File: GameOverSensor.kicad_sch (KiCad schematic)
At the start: 20 parts

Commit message: Changes Serial Port connector to match esp-prog
Both esp-prog and the tag connect cable use even/odd numbering for the
two row connector.
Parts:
- removed J?: Serial Port, symbol Connector_Generic:Conn_02x03_Counter_Clockwise
- added J?: Serial Port, symbol Connector_Generic:Conn_02x03_Odd_Even
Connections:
- net +3V3: now also J?.2 (Pin_2)
- net ESP_BOOT: now also J?.6 (Pin_6)
- net ESP_EN: now also J?.1 (Pin_1)
- net ESP_RX: now also J?.5 (Pin_5)
- net ESP_TX: now also J?.3 (Pin_3)
- net GND: now also J?.4 (Pin_4)

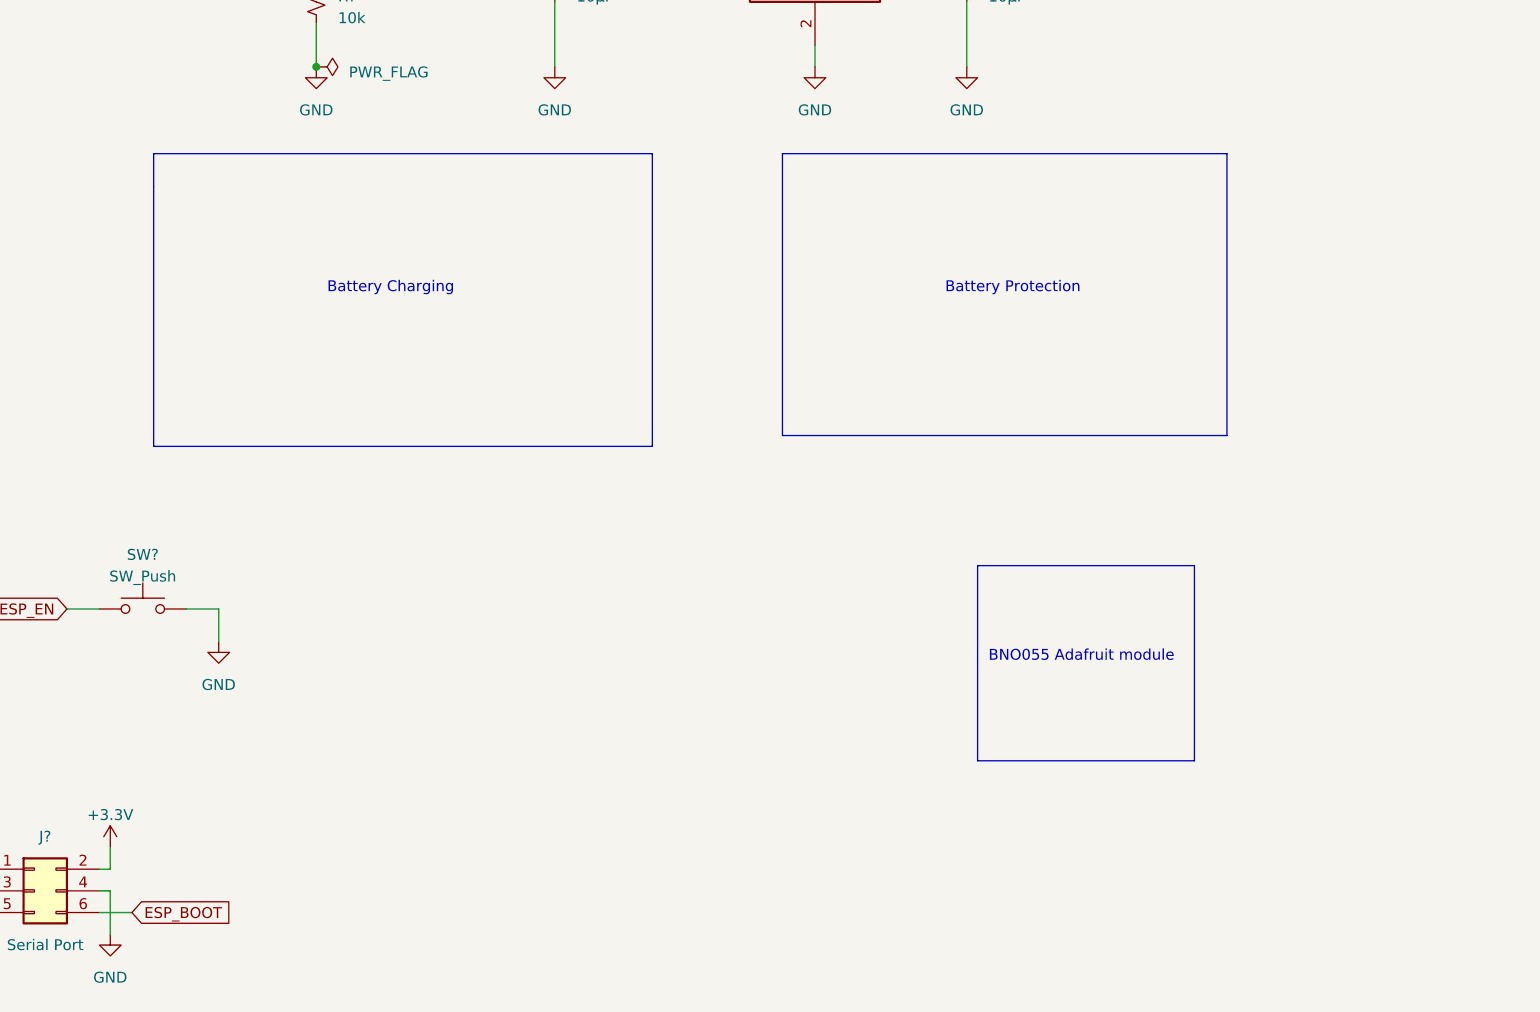
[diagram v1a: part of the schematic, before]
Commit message: Adds battery charging circuit with an MCP73831
The battery will be 400mA, which means we should use 200mA to charge the
battery. This would mean a 5kΩ prog resistor. A 5.1kΩ resistor was
chosen instead to simplify the BOM since we'll already use some of those
in the USB configuration. This means a charging current of approximately
196mA.
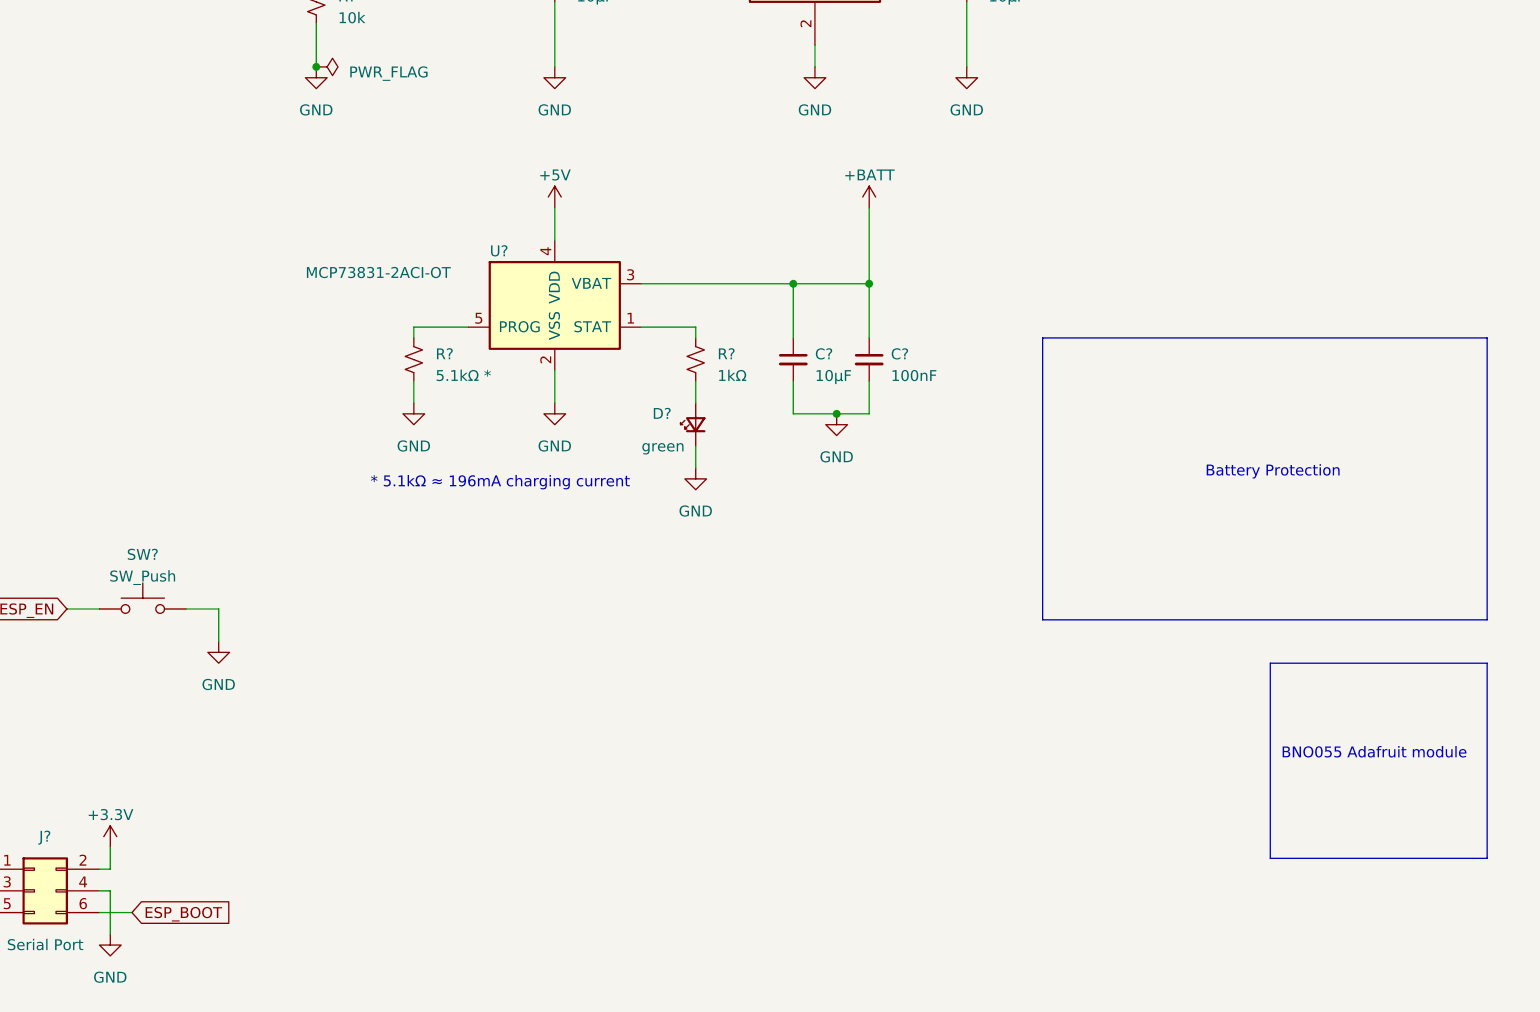
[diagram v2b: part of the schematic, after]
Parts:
- added C?: 10µF, symbol Device:C_Small
- added C?: 100nF, symbol Device:C_Small
- added D?: green, symbol Device:LED_Small
- added R?: 5.1kΩ *, symbol Device:R_Small_US
- added R?: 1kΩ, symbol Device:R_Small_US
- added U?: MCP73831-2ACI-OT, Package_TO_SOT_SMD:SOT-23-5, symbol Battery_Management:MCP73831-2-OT
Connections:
- net +5V: now also U?.4 (VDD)
- net +BATT: now also C?.1, C?.1, U?.3 (VBAT)
- net GND: now also C?.2, C?.2, D?.1 (K), R?.2, U?.2 (VSS)
- new net: R?.1, U?.5 (PROG)
- new net: R?.1, U?.1 (STAT)
- new net: D?.2 (A), R?.2
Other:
- note added: "* 5.1kΩ ≈ 196mA charging current"
- note removed: "Battery Charging"

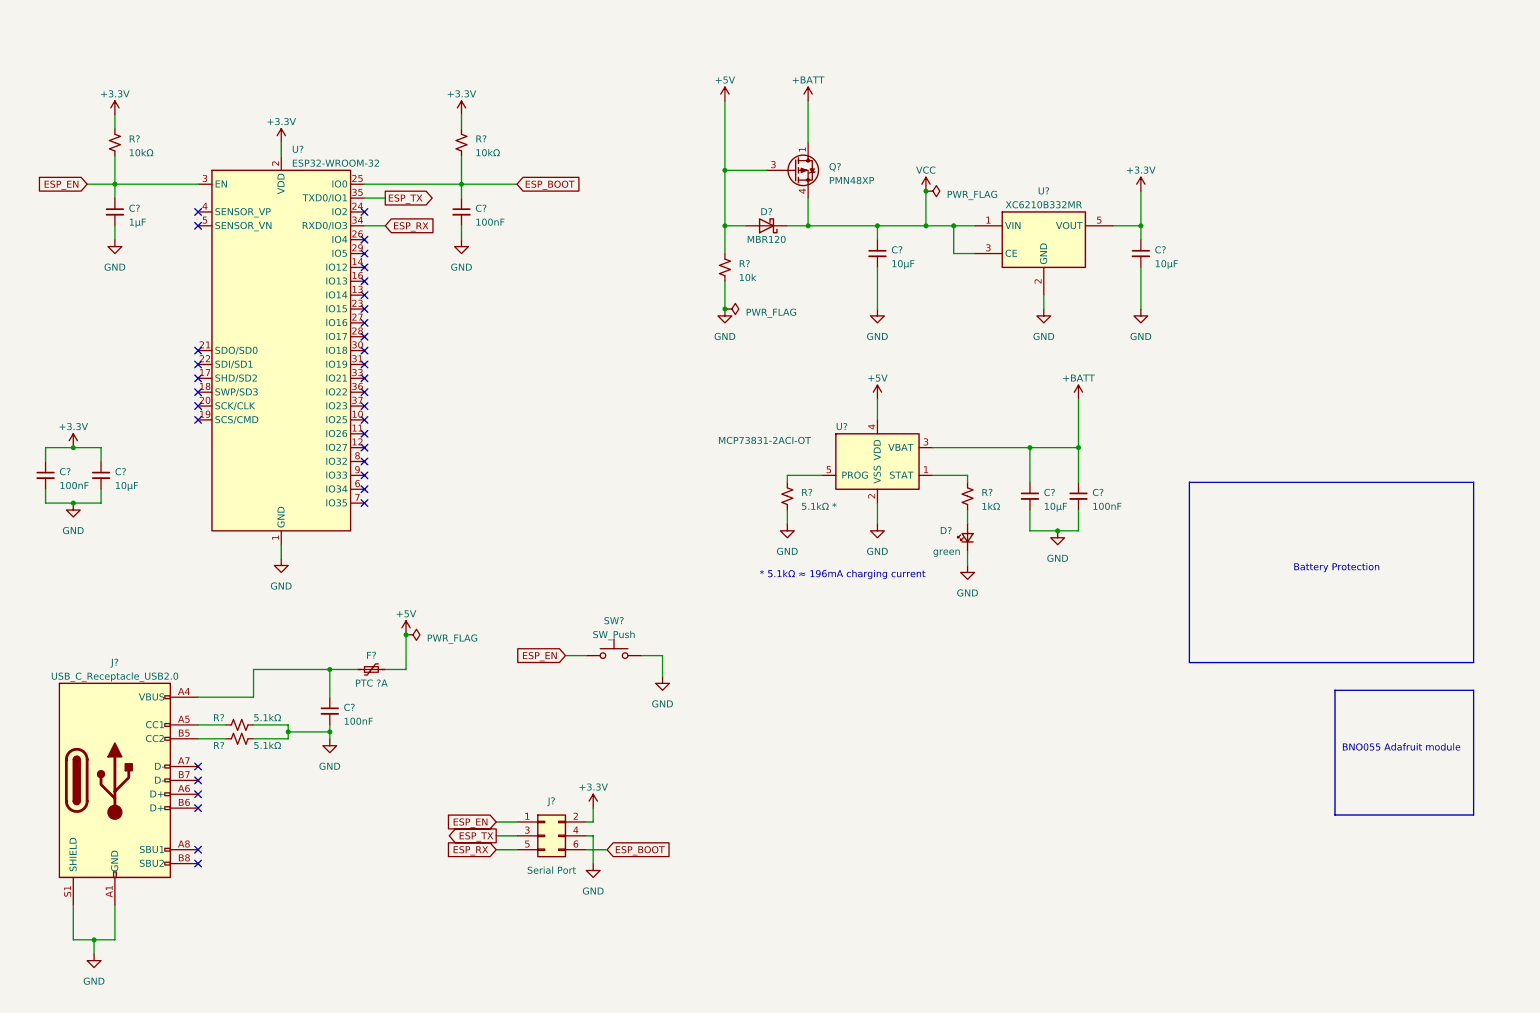
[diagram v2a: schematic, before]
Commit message: Uses battery protection circuit around a BQ29703
This IC has a over current during discharge threshold voltage of 0.160V.
Using the DMG9926UDM MOSFETs, which have a Rds(on) of 0.032A each
(0.064A in total), we would have a cutoff current of 2.5A. If we need
this to be lower, we need to add a resistor in series with the MOSFETs
to increase the voltage difference between VSS and V- in case of
overcurrent.
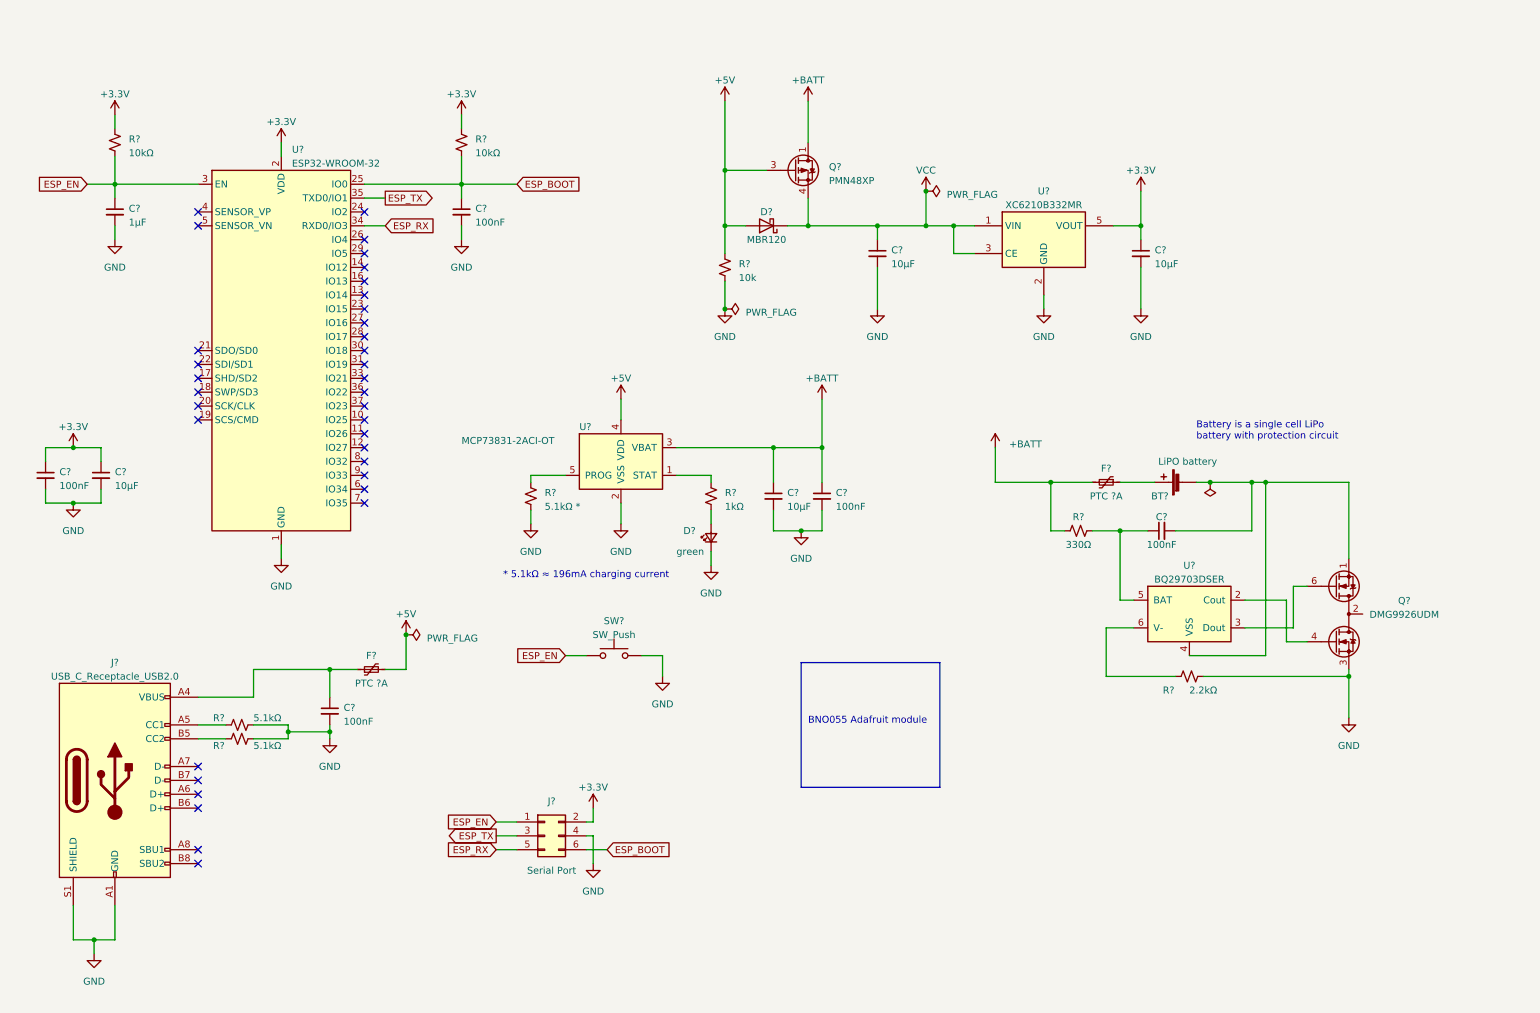
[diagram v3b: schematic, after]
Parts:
- added BT?: LiPO battery, symbol Device:Battery_Cell
- added C?: 100nF, symbol Device:C_Small
- added F?: PTC ?A, symbol Device:Polyfuse_Small
- added Q?: DMG9926UDM, Package_TO_SOT_SMD:SOT-23-6, symbol Transistor_FET:DMG9926UDM
- added R?: 2.2kΩ, symbol Device:R_Small_US
- added R?: 330Ω, symbol Device:R_Small_US
- added U?: BQ29703DSER, Package_SON:WSON-6_1.5x1.5mm_P0.5mm, symbol Battery_Management:BQ297xy
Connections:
- net +BATT: now also F?.2, R?.2
- net GND: now also Q?.3 (S2), R?.2
- new net: BT?.1 (+), F?.1
- new net: R?.1, U?.6 (V-)
- new net: BT?.2 (-), C?.2, Q?.1 (D1), U?.4 (VSS)
- new net: Q?.4 (G2), U?.2 (Cout)
- new net: Q?.6 (G1), U?.3 (Dout)
- new net: C?.1, R?.1, U?.5 (BAT)
- new net: Q?.2 (S1/D2), Q?.5 (S1/D2)
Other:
- note added: "Battery is a single cell LiPo battery with protection circuit"
- note removed: "Battery Protection"
- moved on the sheet: C?, D?, R?, U?

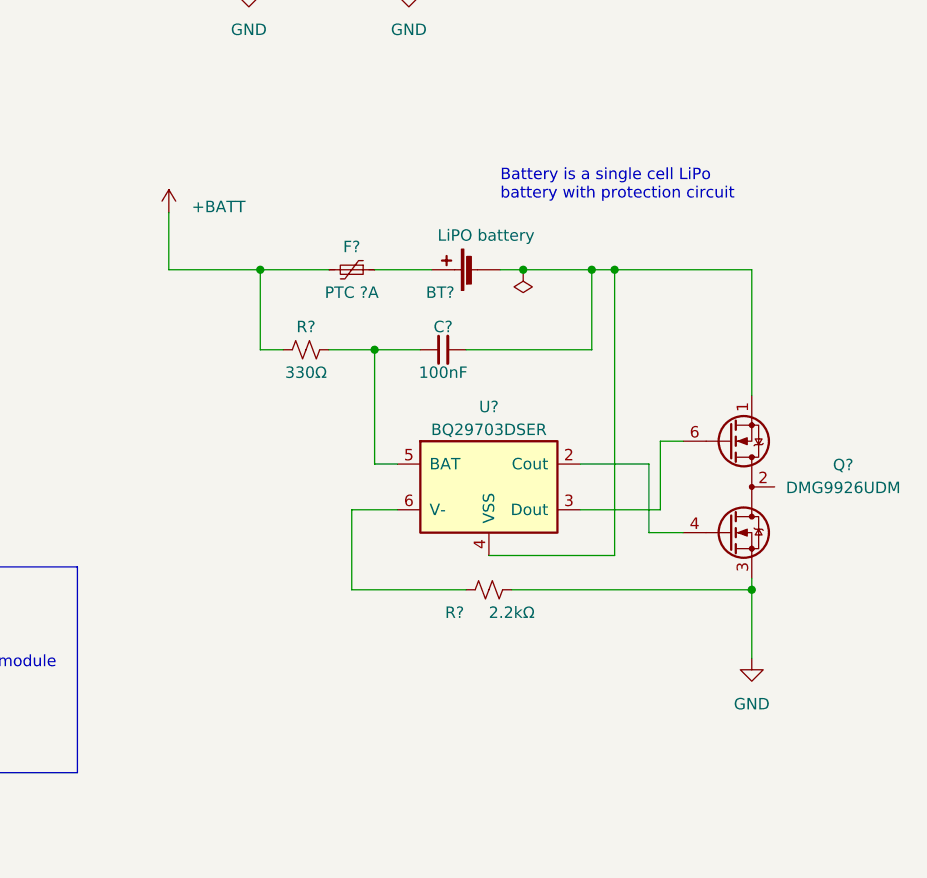
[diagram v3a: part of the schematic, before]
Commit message: Removes on board battery protection circuit
We decided we will only use battery packs that include their own
protection mechanism, so we don't need to do it onboard also.

We still kept the fuse as an extra protection for overcurrent.
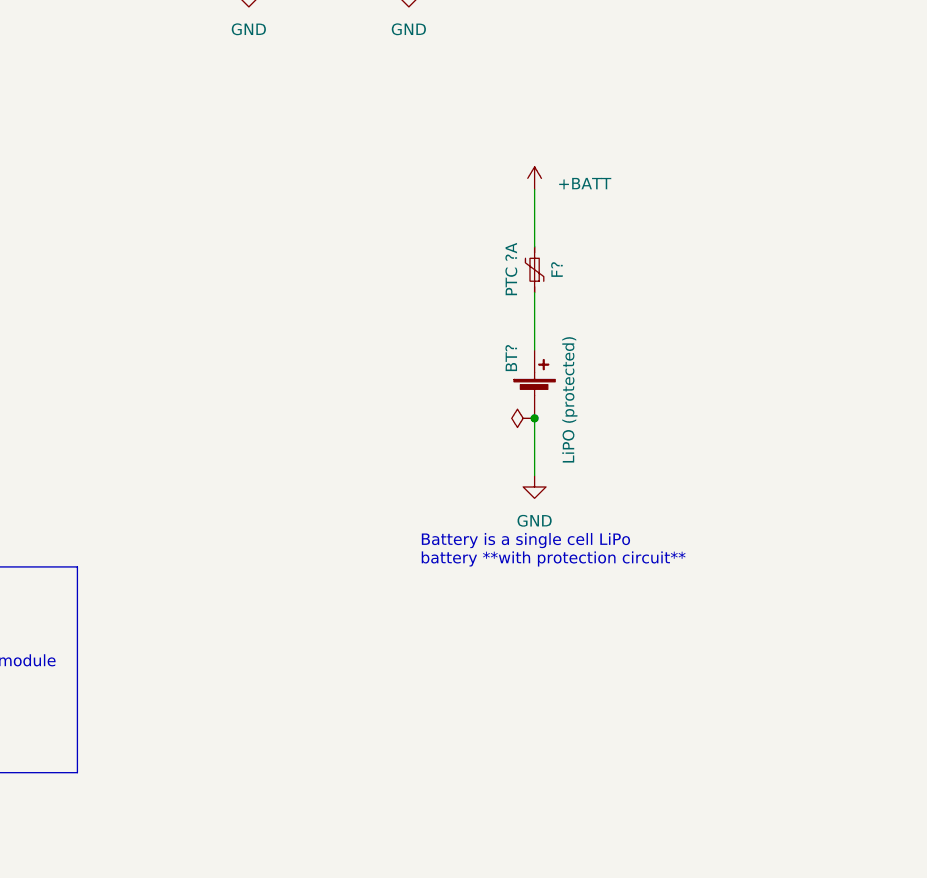
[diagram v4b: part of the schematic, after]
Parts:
- removed C?: 100nF, symbol Device:C_Small
- removed Q?: DMG9926UDM, Package_TO_SOT_SMD:SOT-23-6, symbol Transistor_FET:DMG9926UDM
- removed R?: 2.2kΩ, symbol Device:R_Small_US
- removed R?: 330Ω, symbol Device:R_Small_US
- removed U?: BQ29703DSER, Package_SON:WSON-6_1.5x1.5mm_P0.5mm, symbol Battery_Management:BQ297xy
- BT?: value LiPO battery -> LiPO (protected)
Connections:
- net GND: now also BT?.2 (-)
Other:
- note added: "Battery is a single cell LiPo battery **with protection circuit**"
- note removed: "Battery is a single cell LiPo battery with protection circuit"
- moved on the sheet: BT?, F?
